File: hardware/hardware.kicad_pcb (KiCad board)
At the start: 2 copper layers, 101.6 x 76.2 mm, 5 parts, among them U2 Teensy4.1_DEV-16771, U3 OKI-78SR-3.3_1.5-W36H-C, U4 LT1910, U5 LT1910, U6 LT1910

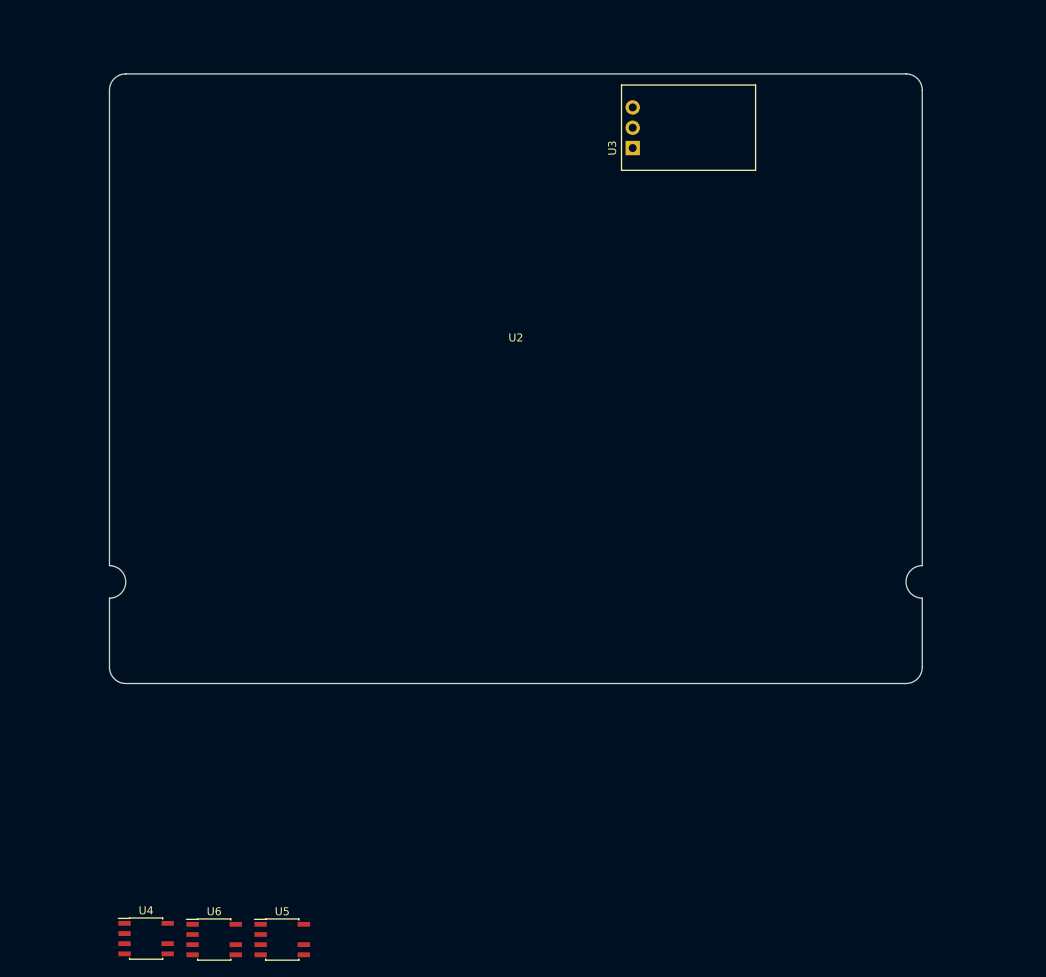
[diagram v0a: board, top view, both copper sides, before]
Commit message: Arranged components on layout
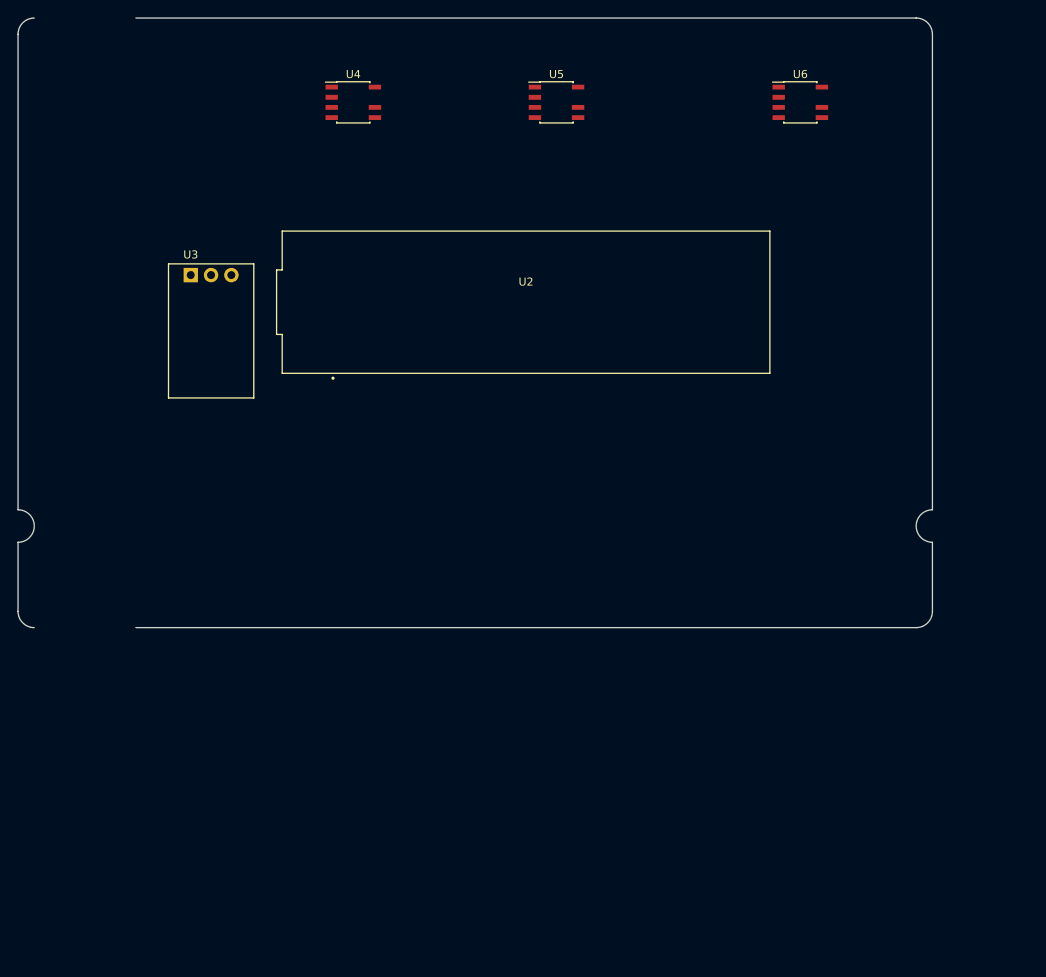
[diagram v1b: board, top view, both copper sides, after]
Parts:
- moved U6 127.8 mm to (148.6, 62.2)
- moved U5 110.1 mm to (118.1, 62.2)
- moved U4 107.7 mm to (92.7, 62.2)
- moved U3 57.5 mm to (72.4, 83.8), turned to 0 degrees
- moved U2 7.10 mm to (63.5, 51.7)
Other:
- board size 101.6 x 76.2 mm -> 114.3 x 76.2 mm

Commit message: Added ground and traces
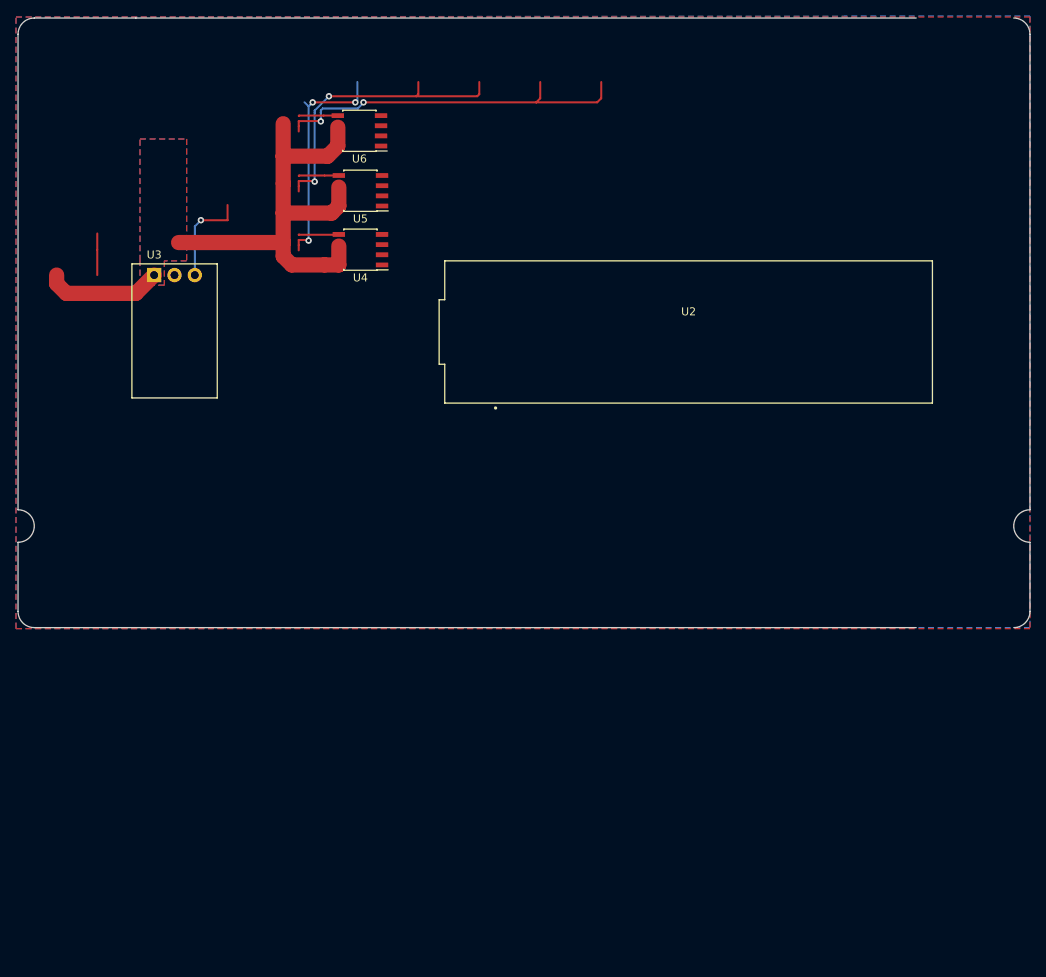
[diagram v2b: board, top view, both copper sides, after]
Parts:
- moved U6 55.2 mm to (93.5, 65.8), turned to 180 degrees
- moved U5 26.9 mm to (93.6, 73.3), turned to 180 degrees
- moved U2 20.7 mm to (83.8, 55.4)
- moved U4 18.4 mm to (93.6, 80.6), turned to 180 degrees
- moved U3 4.57 mm to (67.8, 83.8)
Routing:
- net +12V: track 0.00 -> 73.5 mm
- net Net-(Conn10-Pad1): track 0.00 -> 45.9 mm, vias 0 -> 2
- net Net-(Conn7-Pad1): track 0.00 -> 37.0 mm, vias 0 -> 2
- net Net-(Conn4-Pad1): track 0.00 -> 28.8 mm, vias 0 -> 3
- net +3V3: track 0.00 -> 12.4 mm, vias 0 -> 1
- net +5V: track 0.00 -> 5.21 mm
- net Net-(Q1-Pad4): track 0.00 -> 5.09 mm
- net Net-(Q2-Pad4): track 0.00 -> 5.03 mm
- net Net-(Q3-Pad4): track 0.00 -> 4.90 mm
- added copper zone on B.Cu, net +12V
- added copper zone on F.Cu, net +12V
- added copper zone on B.Cu, net GND
- added copper zone on F.Cu, net GND
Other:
- board size 114.3 x 76.2 mm -> 126.5 x 76.2 mm

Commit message: Worked on layout
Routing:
- net +3V3: track 12.4 -> 222.7 mm, vias 1 -> 6
- net +5V: track 5.21 -> 109.3 mm, vias 0 -> 6
- net /Mosfets and Sensors/pair3_in: track 0.00 -> 68.7 mm, vias 0 -> 1
- net /Mosfets and Sensors/pair2_in: track 0.00 -> 52.9 mm, vias 0 -> 1
- net /Mosfets and Sensors/pair1_in: track 0.00 -> 35.6 mm, vias 0 -> 1
- net /Mosfets and Sensors/pair1_out: track 0.00 -> 30.1 mm, vias 0 -> 2
- net /Mosfets and Sensors/pair3_out: track 0.00 -> 27.5 mm, vias 0 -> 1
- net /Mosfets and Sensors/pair2_out: track 0.00 -> 26.7 mm, vias 0 -> 1
- net Net-(C1-Pad1): track 0.00 -> 15.4 mm
- net Net-(C1-Pad2): track 0.00 -> 4.60 mm
- net Net-(C12-Pad1): track 0.00 -> 3.20 mm
- net Net-(R3-Pad2): track 0.00 -> 3.15 mm
- net Net-(C8-Pad1): track 0.00 -> 3.05 mm
- net Net-(C10-Pad1): track 0.00 -> 2.97 mm
- net Net-(Conn4-Pad1): track 28.8 -> 31.7 mm
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
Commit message: Finished layout?
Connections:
- U4 pad 6: +12V -> +12VA
- U4 pad 8: +12V -> +12VA
- U5 pad 6: +12V -> +12VA
- U5 pad 8: +12V -> +12VA
- U6 pad 6: +12V -> +12VA
- U6 pad 8: +12V -> +12VA
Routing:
- net +12VA: track 0.00 -> 62.5 mm
- net +12V: track 73.5 -> 14.7 mm
- net Net-(Conn4-Pad1): track 31.7 -> 40.1 mm, vias 3 -> 2
- net +3V3: track 222.7 -> 216.9 mm
- net +5V: track 109.3 -> 114.0 mm
- net Net-(Conn7-Pad1): track 37.0 -> 38.4 mm

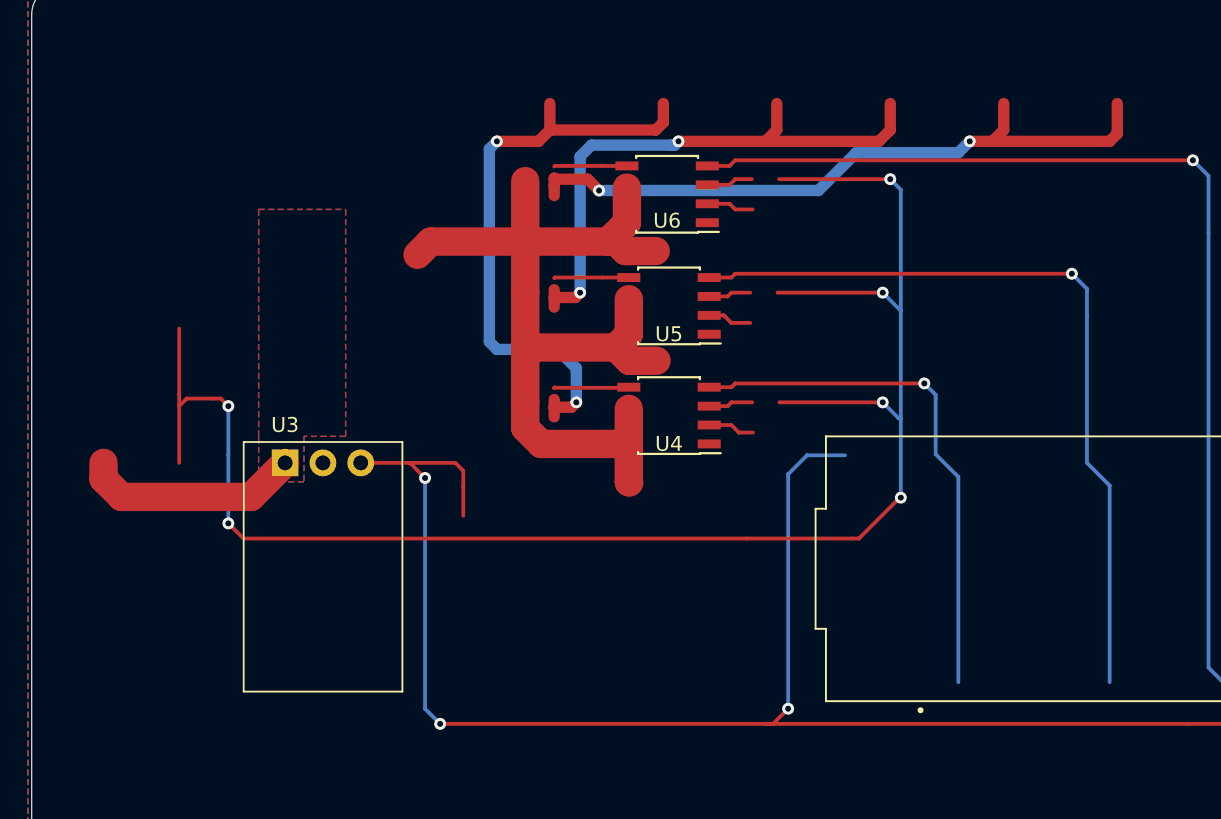
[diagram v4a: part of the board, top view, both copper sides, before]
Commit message: Increased trace sizes
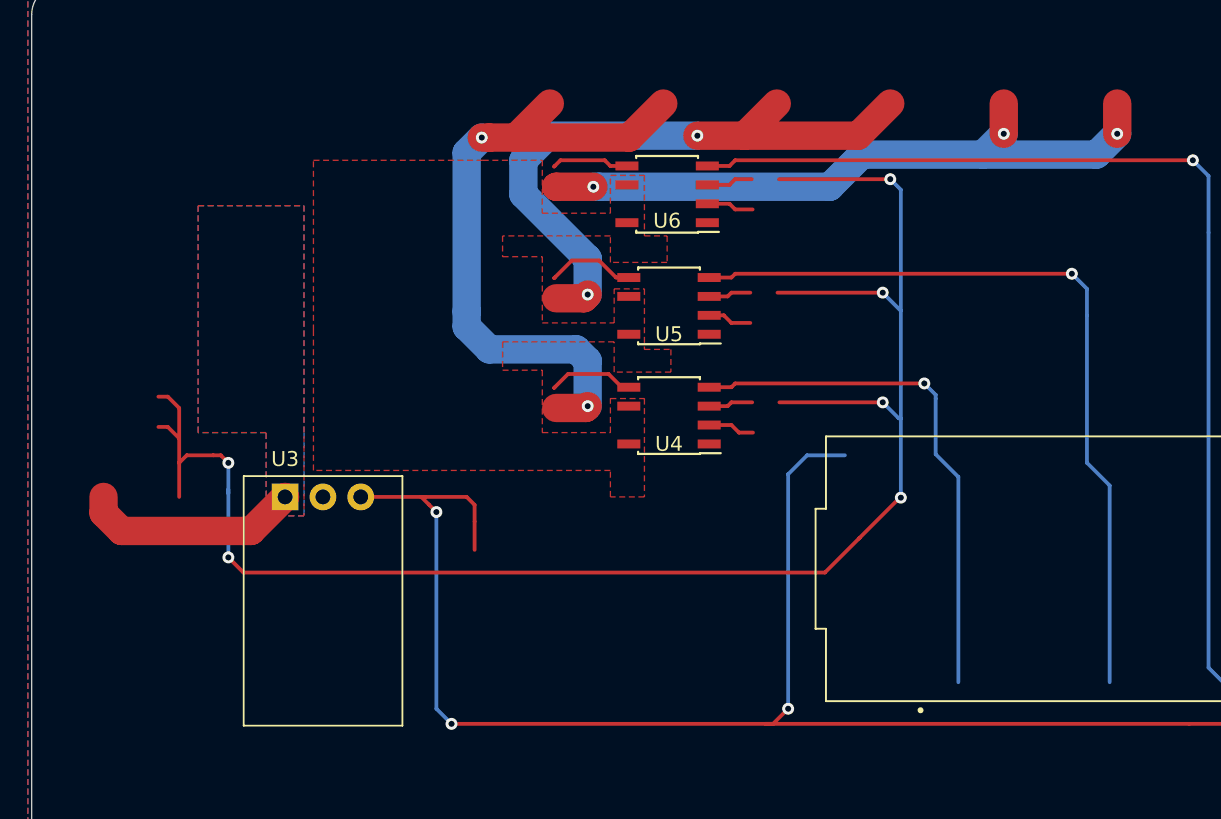
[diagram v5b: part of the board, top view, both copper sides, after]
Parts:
- moved U3 2.29 mm to (67.8, 86.1)
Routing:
- net +12VA: track 62.5 -> 0.00 mm
- net Net-(Conn7-Pad1): track 38.4 -> 42.3 mm
- net Net-(Conn4-Pad1): track 40.1 -> 43.8 mm
- net +3V3: track 216.9 -> 214.9 mm
- net Net-(Q2-Pad4): track 5.03 -> 6.03 mm
- net Net-(Q1-Pad4): track 5.09 -> 5.88 mm
- net Net-(Conn10-Pad1): track 45.8 -> 45.2 mm, vias 2 -> 3
- added copper zone on F.Cu, net +12VA

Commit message: CDR Changes
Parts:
- added Bottom Text: MRDT, MRDT_Silkscreens:0_MRDT_Logo_20mm, F.Cu at (165.1, 113.5)
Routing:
- net Net-(C1-Pad2): track 4.60 -> 36.8 mm, vias 0 -> 2
- net Net-(J1-Pad4): track 0.00 -> 29.9 mm
- net +3V3: track 214.9 -> 231.6 mm, vias 6 -> 8
- net Net-(J1-Pad2): track 0.00 -> 11.9 mm
- net Net-(J1-Pad1): track 0.00 -> 11.9 mm
- net Net-(J1-Pad5): track 0.00 -> 6.30 mm
- net Net-(J1-Pad6): track 0.00 -> 6.22 mm
- net Net-(C1-Pad1): track 15.4 -> 20.2 mm
